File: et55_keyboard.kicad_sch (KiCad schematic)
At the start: 64 parts

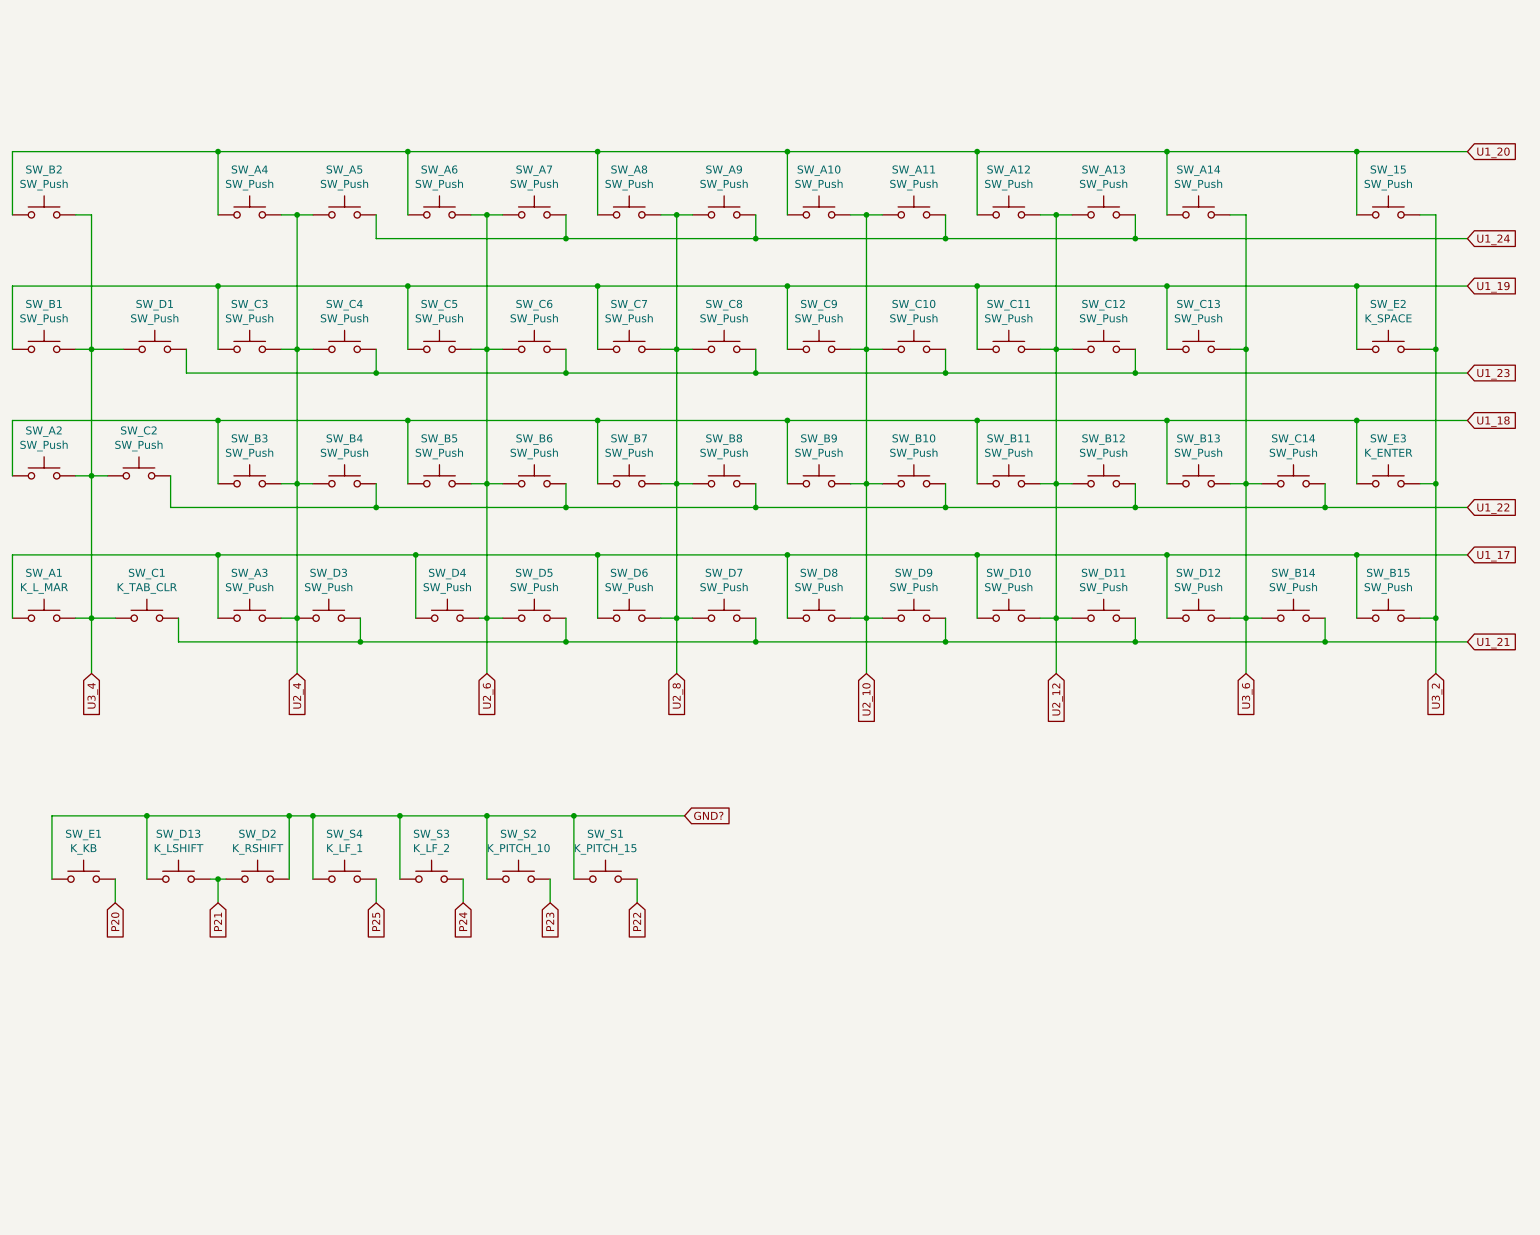
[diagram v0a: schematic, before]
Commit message: fix: connect cpu pins to keyboard matrix
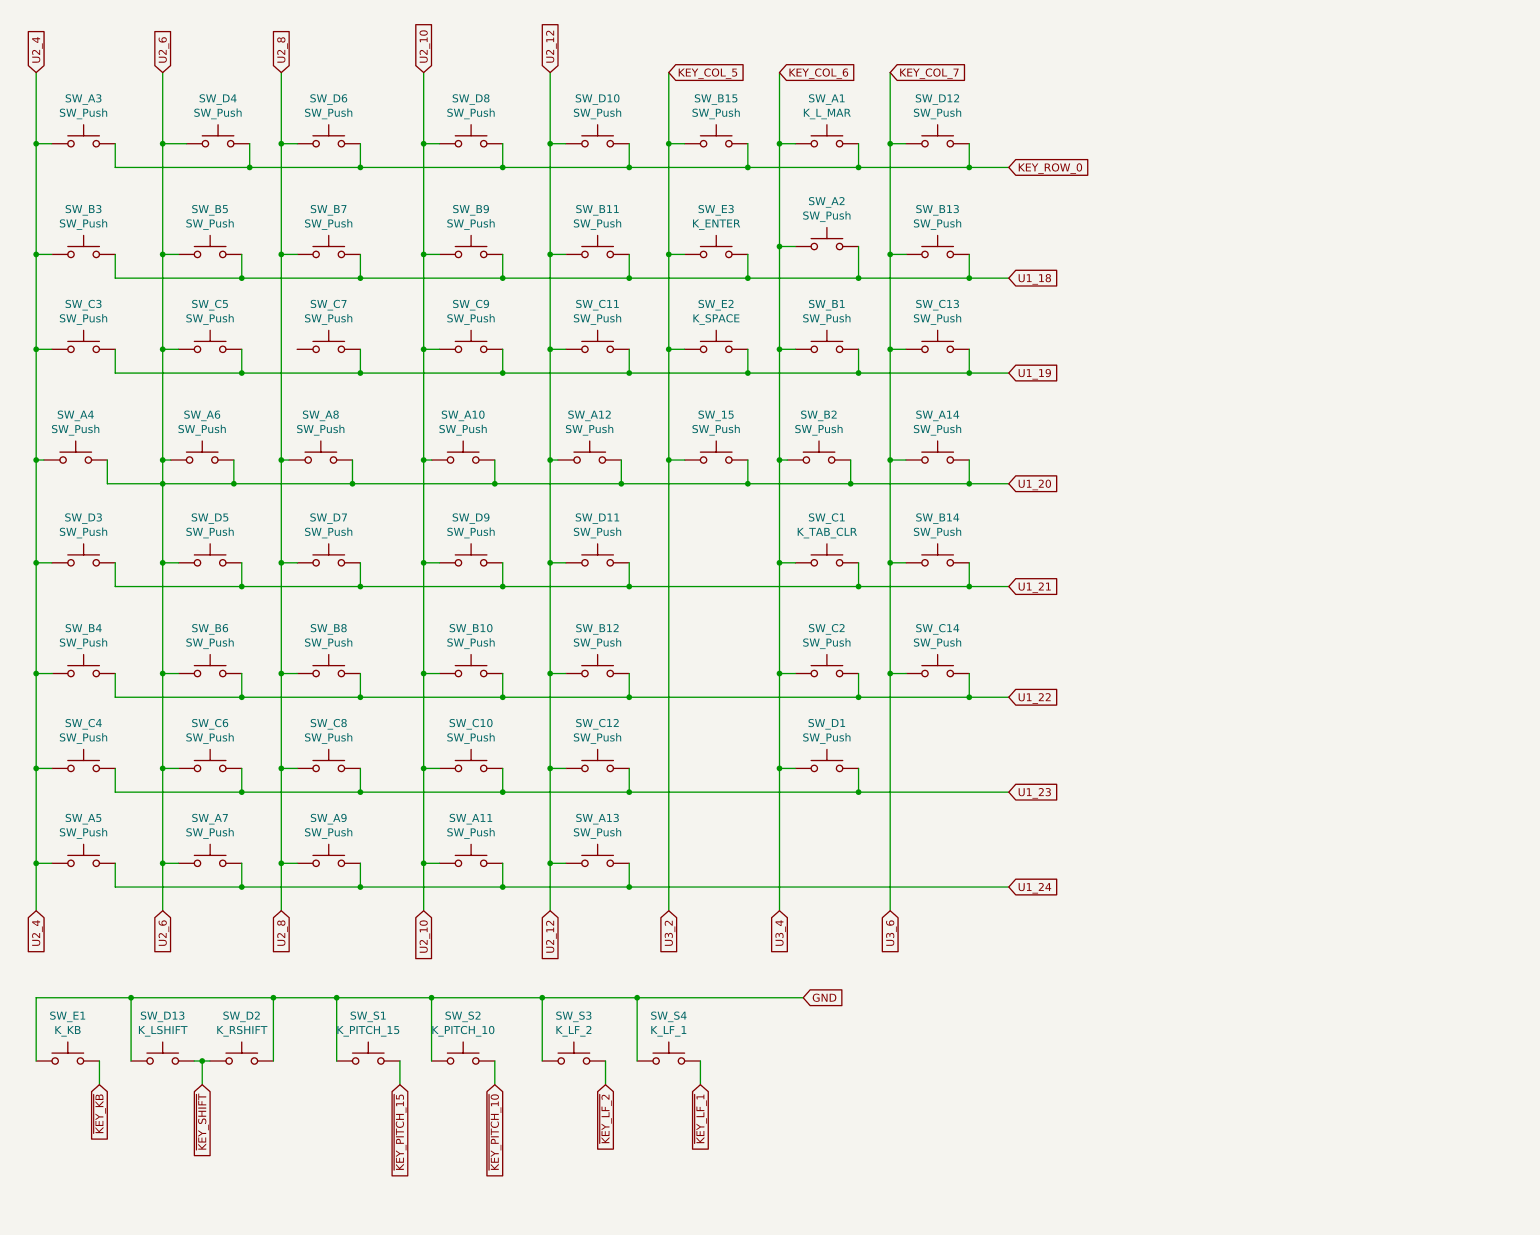
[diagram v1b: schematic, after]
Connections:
- net U1_18: now also SW_A2.2, SW_B11.2, SW_B13.2, SW_B3.2, SW_B5.2, SW_B7.2, SW_B9.2, SW_E3.2; no longer SW_A2.1, SW_B11.1, SW_B13.1, SW_B3.1, SW_B5.1, SW_B7.1, SW_B9.1, SW_E3.1
- net U1_19: now also SW_B1.2, SW_C11.2, SW_C13.2, SW_C3.2, SW_C5.2, SW_C7.2, SW_C9.2, SW_E2.2; no longer SW_B1.1, SW_C11.1, SW_C13.1, SW_C3.1, SW_C5.1, SW_C7.1, SW_C9.1, SW_E2.1
- net U1_20: now also SW_15.2, SW_A10.2, SW_A12.2, SW_A14.2, SW_A4.2, SW_A6.2, SW_A7.1, SW_A8.2, SW_B2.2, SW_B5.1, SW_B6.1, SW_C5.1, SW_C6.1, SW_D4.1, SW_D5.1; no longer SW_15.1, SW_A10.1, SW_A12.1, SW_A14.1, SW_A4.1, SW_A8.1, SW_B2.1
- net U2_10: now also SW_A10.1, SW_B9.1, SW_C9.1, SW_D8.1; no longer SW_A10.2, SW_B9.2, SW_C9.2, SW_D8.2
- net U2_12: now also SW_A12.1, SW_B11.1, SW_C11.1, SW_D10.1; no longer SW_A12.2, SW_B11.2, SW_C11.2, SW_D10.2
- net U2_4: now also SW_A3.1, SW_A4.1, SW_B3.1, SW_C3.1; no longer SW_A3.2, SW_A4.2, SW_B3.2, SW_C3.2
- net U2_8: now also SW_A8.1, SW_B7.1, SW_D6.1; no longer SW_A8.2, SW_B7.2, SW_C7.2, SW_D6.2
- net GND? renamed GND
- net P20 renamed ~{KEY_KB}
- net P21 renamed ~{KEY_SHIFT}
- net P22 renamed ~{KEY_PITCH_15}
- net P23 renamed ~{KEY_PITCH_10}
- net P24 renamed ~{KEY_LF_2}
- net P25 renamed ~{KEY_LF_1}
- removed net U1_17: SW_A1.1, SW_A3.1, SW_B15.1, SW_D10.1, SW_D12.1, SW_D4.1, SW_D6.1, SW_D8.1
- removed net U2_6: SW_A6.2, SW_A7.1, SW_B5.2, SW_B6.1, SW_C5.2, SW_C6.1, SW_D4.2, SW_D5.1
- removed net U3_2: SW_15.2, SW_B15.2, SW_E2.2, SW_E3.2
- removed net U3_4: SW_A1.2, SW_A2.2, SW_B1.2, SW_B2.2, SW_C1.1, SW_C2.1, SW_D1.1
- removed net U3_6: SW_A14.2, SW_B13.2, SW_B14.1, SW_C13.2, SW_C14.1, SW_D12.2
- new net KEY_COL_5: SW_15.1, SW_B15.1, SW_E2.1, SW_E3.1
- new net KEY_COL_6: SW_A1.1, SW_A2.1, SW_B1.1, SW_B2.1, SW_C1.1, SW_C2.1, SW_D1.1
- new net KEY_COL_7: SW_A14.1, SW_B13.1, SW_B14.1, SW_C13.1, SW_C14.1, SW_D12.1
- new net KEY_ROW_0: SW_A1.2, SW_A3.2, SW_B15.2, SW_D10.2, SW_D12.2, SW_D4.2, SW_D6.2, SW_D8.2
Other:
- moved on the sheet: SW_15, SW_A1, SW_A10, SW_A11, SW_A12, SW_A13, SW_A14, SW_A2, SW_A3, SW_A4, SW_A5, SW_A6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
